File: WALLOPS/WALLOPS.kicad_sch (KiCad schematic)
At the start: 19 parts, among them J1 JST-PH 1x9 Connector - WALLOP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, Q1 AO3401A, U1 VL53L8CX 0 (Zwicky), U2 VL58L8CX 1 (Aristotle), U3 VL53L8CX 3 (Copernicus), U4 VL53L8CX 2 (Brahe), U5 6DOF IMU (Sisko), U6 5V to 3.3V Converter

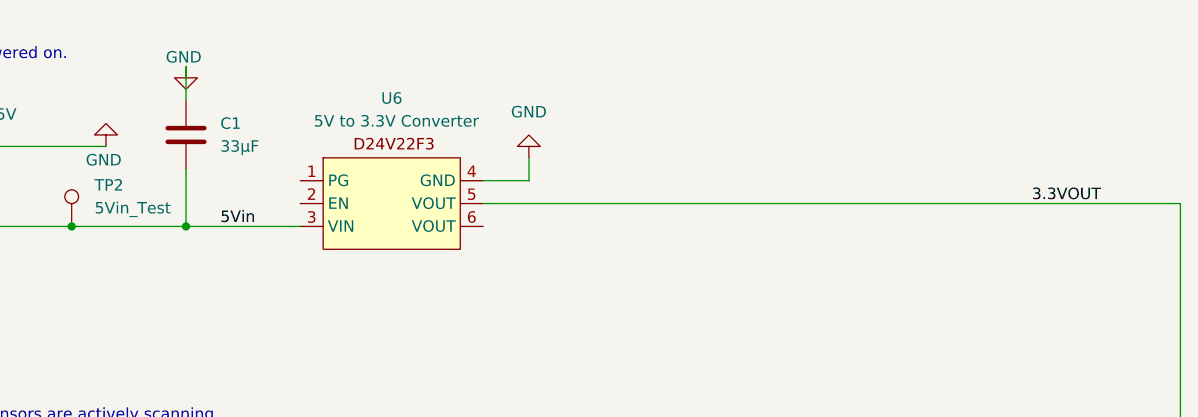
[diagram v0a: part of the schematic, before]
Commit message: Updated capacitors to filter noise and added magnetometer
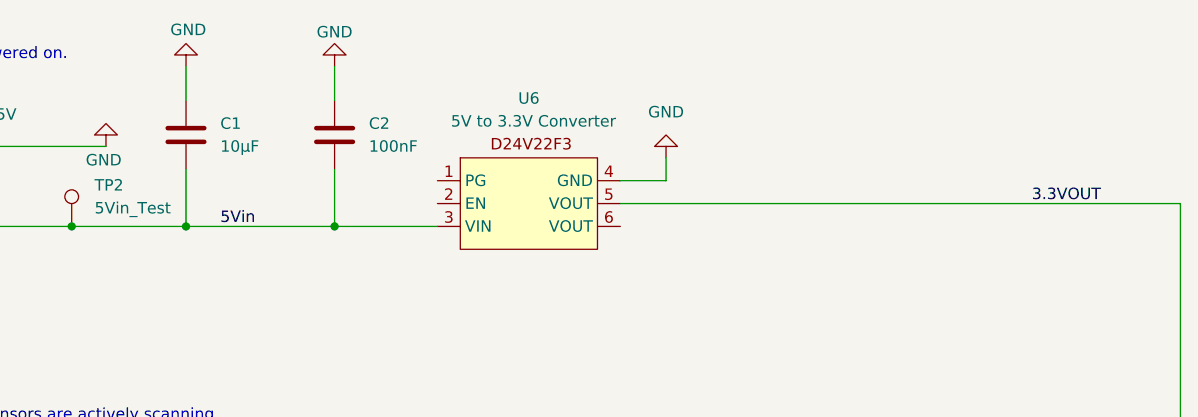
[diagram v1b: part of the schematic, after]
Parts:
- added C2: 100nF, symbol Device:C
- C1: value 33µF -> 10µF
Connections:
- net 5Vin: now also C2.2
- net GND: now also C2.1
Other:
- moved on the sheet: U6
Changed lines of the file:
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@@
 	)
 	(junction
+		(at 153.67 43.18)
+		(diameter 0)
+		(color 0 0 0 0)
+	)
+	(junction
 		(at 90.17 81.28)
 		(diameter 0)
@@
 	(wire
 		(pts
-			(xy 170.18 40.64) (xy 247.65 40.64)
+			(xy 185.42 40.64) (xy 247.65 40.64)
 		)
 		(stroke
@@
 	(wire
 		(pts
+			(xy 153.67 43.18) (xy 165.1 43.18)
+		)
+		(stroke
+			(width 0)
+			(type default)
+		)
+	)
+	(wire
+		(pts
 			(xy 82.55 81.28) (xy 90.17 81.28)
 		)
@@
 	(wire
 		(pts
-			(xy 175.26 35.56) (xy 175.26 38.1)
+			(xy 190.5 35.56) (xy 190.5 38.1)
 		)
 		(stroke
@@
 	(wire
 		(pts
+			(xy 153.67 36.83) (xy 153.67 43.18)
+		)
+		(stroke
+			(width 0)
+			(type default)
+		)
+	)
+	(wire
+		(pts
 			(xy 113.03 100.33) (xy 113.03 101.6)
 		)
@@
 	(wire
 		(pts
+			(xy 153.67 25.4) (xy 153.67 29.21)
+		)
+		(stroke
+			(width 0)
+			(type default)
+		)
+	)
+	(wire
+		(pts
 			(xy 26.67 63.5) (xy 33.02 63.5)
 		)
@@
 	(wire
 		(pts
-			(xy 170.18 38.1) (xy 175.26 38.1)
+			(xy 185.42 38.1) (xy 190.5 38.1)
 		)
 		(stroke
@@
 	(wire
 		(pts
-			(xy 137.16 43.18) (xy 149.86 43.18)
+			(xy 137.16 43.18) (xy 153.67 43.18)
 		)
 		(stroke
@@
 	)
 	(symbol
+		(lib_id "power:GND")
+		(at 153.67 25.4 180)
+		(unit 1)
+		(exclude_from_sim no)
+		(in_bom yes)
+		(on_board yes)
+		(dnp no)
+		(property "Reference" "#PWR03"
+			(at 153.67 19.05 0)
+			(effects
+				(font
+					(size 1.27 1.27)
+				)
+				(hide yes)
+			)
+		)
+		(property "Value" "GND"
+			(at 153.67 21.59 0)
+			(effects
+				(font
+					(size 1.27 1.27)
+				)
+			)
+		)
+		(property "Footprint" ""
+			(at 153.67 25.4 0)
+			(effects
+				(font
+					(size 1.27 1.27)
+				)
+				(hide yes)
+			)
+		)
+		(property "Datasheet" ""
+			(at 153.67 25.4 0)
+			(effects
+				(font
+					(size 1.27 1.27)
+				)
+				(hide yes)
+			)
+		)
+		(property "Description" "Power symbol creates a global label with name \"GND\" , ground"
+			(at 153.67 25.4 0)
+			(effects
+				(font
+					(size 1.27 1.27)
+				)
+				(hide yes)
+			)
+		)
+		(pin "1"
+		)
+		(instances
+			(project ""
+				(path "/a71b320d-cbec-40c8-adfb-8ac61cfef5bf"
+					(reference "#PWR03")
+					(unit 1)
+				)
+			)
+		)
+	)
+	(symbol
 		(lib_id "Device:C")
 		(at 137.16 33.02 0)
@@
 			)
 		)
-		(property "Value" "33µF"
+		(property "Value" "10µF"
 			(at 140.97 34.2899 0)
 			(effects
@@
 	(symbol
 		(lib_id "power:GND")
-		(at 137.16 25.4 0)
+		(at 137.16 25.4 180)
 		(unit 1)
 		(exclude_from_sim no)
@@
 		(dnp no)
 		(property "Reference" "#PWR04"
-			(at 137.16 31.75 0)
+			(at 137.16 19.05 0)
 			(effects
 				(font
@@
 		)
 		(property "Value" "GND"
-			(at 136.906 24.384 0)
+			(at 137.414 21.336 0)
 			(effects
 				(font
@@
 	)
 	(symbol
+		(lib_id "Device:C")
+		(at 153.67 33.02 0)
+		(unit 1)
+		(exclude_from_sim no)
+		(in_bom yes)
+		(on_board yes)
+		(dnp no)
+		(fields_autoplaced yes)
+		(property "Reference" "C2"
+			(at 157.48 31.7499 0)
+			(effects
+				(font
+					(size 1.27 1.27)
+				)
+				(justify left)
+			)
+		)
+		(property "Value" "100nF"
+			(at 157.48 34.2899 0)
+			(effects
+				(font
+					(size 1.27 1.27)
+				)
+				(justify left)
+			)
+		)
+		(property "Footprint" ""
+			(at 154.6352 36.83 0)
+			(effects
+				(font
+					(size 1.27 1.27)
+				)
+				(hide yes)
+			)
+		)
+		(property "Datasheet" "~"
+			(at 153.67 33.02 0)
+			(effects
+				(font
+					(size 1.27 1.27)
+				)
+				(hide yes)
+			)
+		)
+		(property "Description" "Unpolarized capacitor"
+			(at 153.67 33.02 0)
+			(effects
+				(font
+					(size 1.27 1.27)
+				)
+				(hide yes)
+			)
+		)
+		(pin "2"
+		)
+		(pin "1"
+		)
+		(instances
+			(project ""
+				(path "/a71b320d-cbec-40c8-adfb-8ac61cfef5bf"
+					(reference "C2")
+					(unit 1)
+				)
+			)
+		)
+	)
+	(symbol
 		(lib_id "Device:LED")
 		(at 110.49 73.66 180)
@@
 	(symbol
 		(lib_id "RockSat_Sym:Pololu_D24V22F3")
-		(at 160.02 40.64 0)
+		(at 175.26 40.64 0)
 		(unit 1)
 		(exclude_from_sim no)
@@
 		(dnp no)
 		(property "Reference" "U6"
-			(at 160.02 28.956 0)
+			(at 175.26 28.956 0)
 			(effects
 				(font
@@
 		)
 		(property "Value" "5V to 3.3V Converter"
-			(at 160.528 31.496 0)
+			(at 175.768 31.496 0)
 			(effects
 				(font
@@
 		)
 		(property "Footprint" "RockSat:D24V22F3"
-			(at 160.02 40.64 0)
+			(at 175.26 40.64 0)
 			(effects
 				(font
@@
 		)
 		(property "Datasheet" ""
-			(at 160.02 40.64 0)
+			(at 175.26 40.64 0)
 			(effects
 				(font
@@
 		)
 		(property "Description" ""
-			(at 160.02 40.64 0)
+			(at 175.26 40.64 0)
 			(effects
 				(font
@@
 	(symbol
 		(lib_id "power:GND")
-		(at 175.26 35.56 180)
+		(at 190.5 35.56 180)
 		(unit 1)
 		(exclude_from_sim no)
@@
 		(fields_autoplaced yes)
 		(property "Reference" "#PWR02"
-			(at 175.26 29.21 0)
+			(at 190.5 29.21 0)
 			(effects
 				(font
@@
 		)
 		(property "Value" "GND"
-			(at 175.26 30.48 0)
+			(at 190.5 30.48 0)
 			(effects
 				(font
@@
 		)
 		(property "Footprint" ""
-			(at 175.26 35.56 0)
+			(at 190.5 35.56 0)
 			(effects
 				(font
@@
 		)
 		(property "Datasheet" ""
-			(at 175.26 35.56 0)
+			(at 190.5 35.56 0)
 			(effects
 				(font
@@
 		)
 		(property "Description" "Power symbol creates a global label with name \"GND\" , ground"
-			(at 175.26 35.56 0)
+			(at 190.5 35.56 0)
 			(effects
 				(font

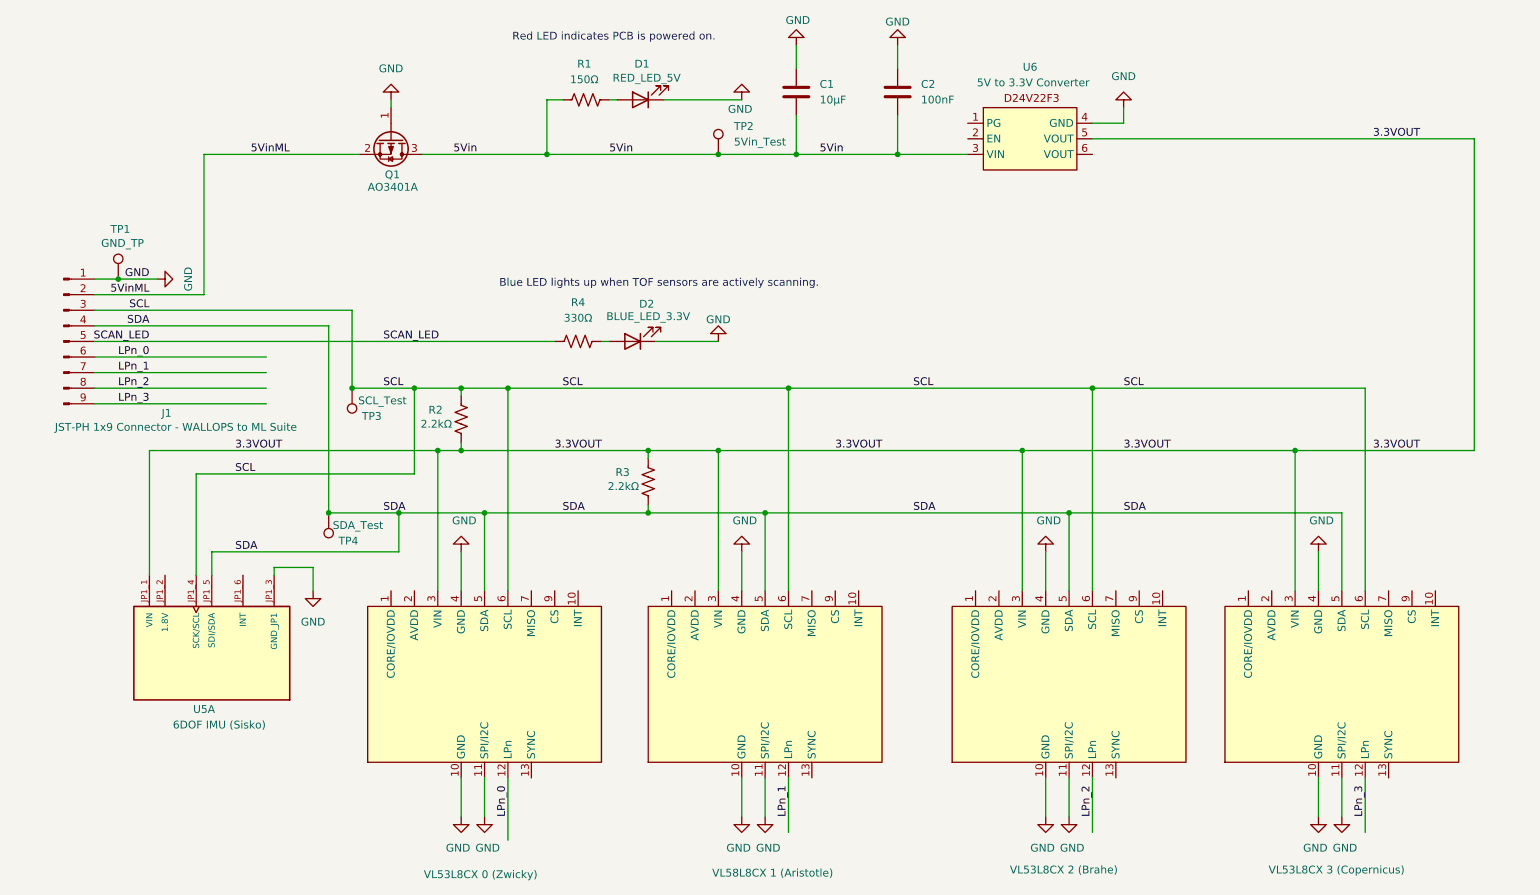
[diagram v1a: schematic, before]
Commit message: Added Magnetometer to schematic
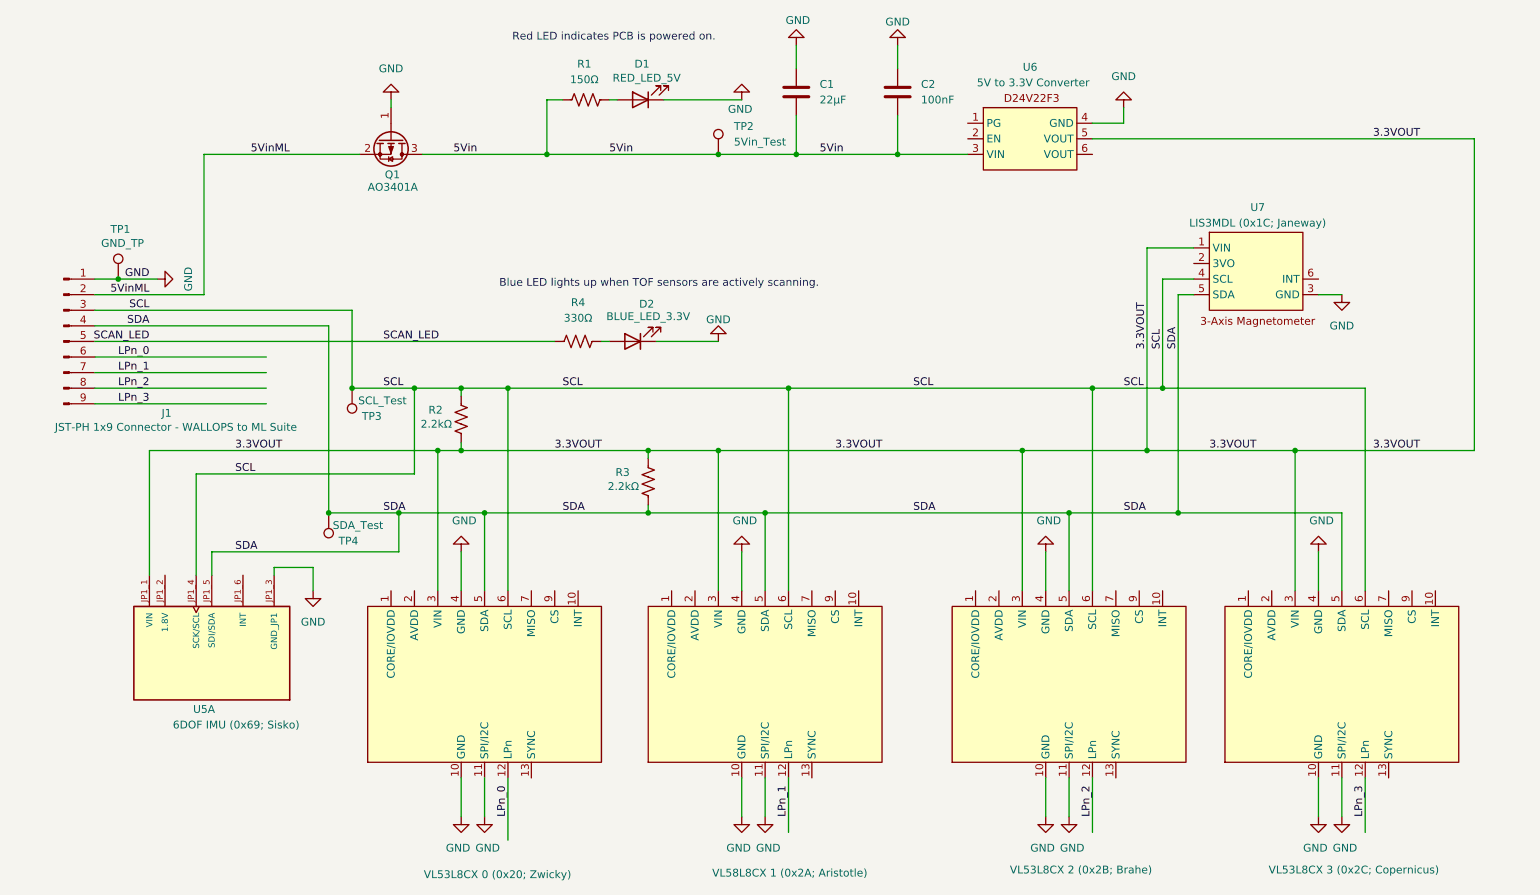
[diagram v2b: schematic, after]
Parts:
- added U7: LIS3MDL (0x1C; Janeway), symbol RockSat_Sym:LIS3MDL_Magnetometer
- C1: value 10µF -> 22µF
- U1: value VL53L8CX 0 (Zwicky) -> VL53L8CX 0 (0x20; Zwicky)
- U2: value VL58L8CX 1 (Aristotle) -> VL58L8CX 1 (0x2A; Aristotle)
- U3: value VL53L8CX 3 (Copernicus) -> VL53L8CX 3 (0x2C; Copernicus)
- U4: value VL53L8CX 2 (Brahe) -> VL53L8CX 2 (0x2B; Brahe)
- U5: value 6DOF IMU (Sisko) -> 6DOF IMU (0x69; Sisko)
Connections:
- net 3.3VOUT: now also U7.1 (VIN)
- net GND: now also U7.3 (GND)
- net SCL: now also U7.4 (SCL)
- net SDA: now also U7.5 (SDA)

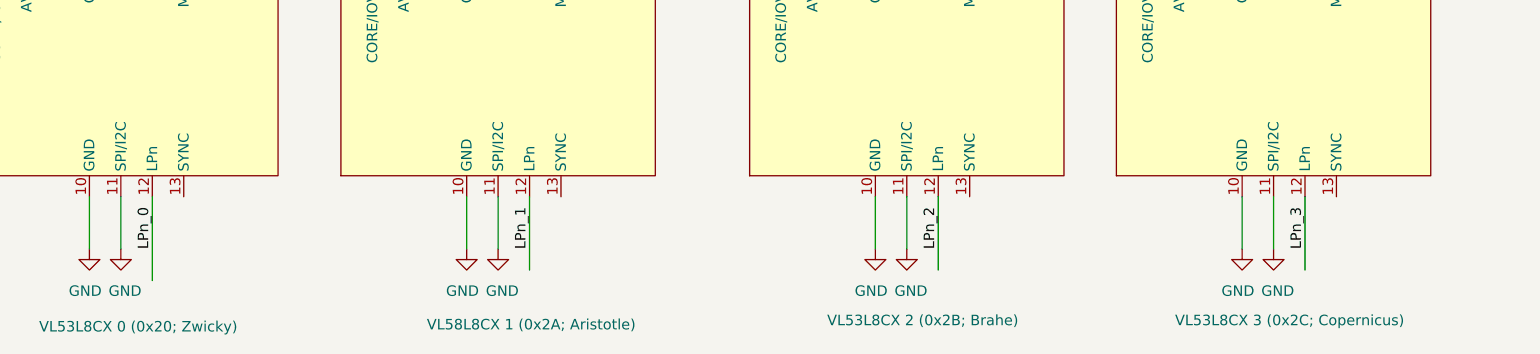
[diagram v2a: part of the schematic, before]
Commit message: Added individual TOF LPn pins to WALLOPS PCB
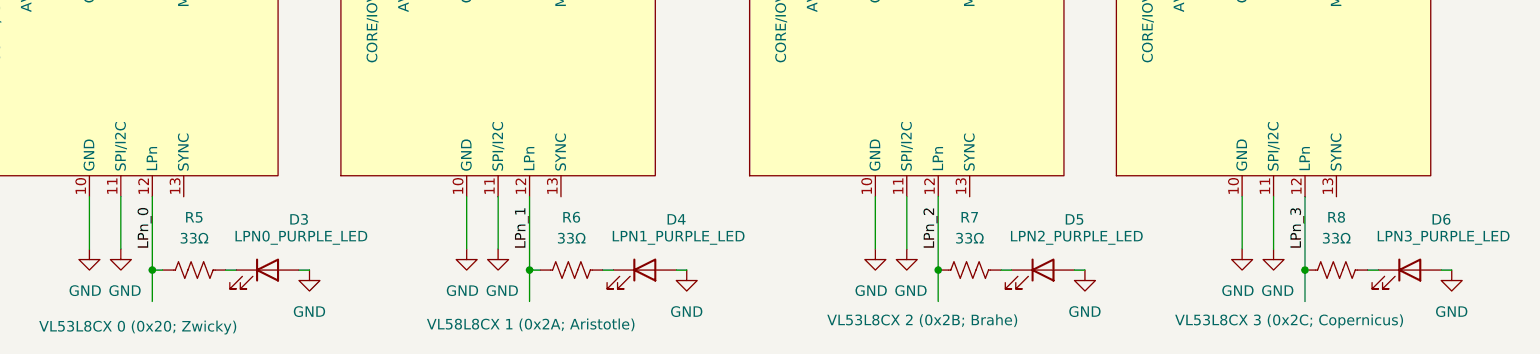
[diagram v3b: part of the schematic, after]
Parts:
- added D3: LPN0_PURPLE_LED, LED_SMD:LED_0201_0603Metric_Pad0.64x0.40mm_HandSolder, symbol Device:LED
- added D4: LPN1_PURPLE_LED, LED_SMD:LED_0201_0603Metric_Pad0.64x0.40mm_HandSolder, symbol Device:LED
- added D5: LPN2_PURPLE_LED, LED_SMD:LED_0201_0603Metric_Pad0.64x0.40mm_HandSolder, symbol Device:LED
- added D6: LPN3_PURPLE_LED, LED_SMD:LED_0201_0603Metric_Pad0.64x0.40mm_HandSolder, symbol Device:LED
- added R5, R6, R7, R8: 33Ω, Resistor_SMD:R_0805_2012Metric_Pad1.20x1.40mm_HandSolder, symbol Device:R_US
- C1: footprint Capacitor_SMD:C_0805_2012Metric -> Capacitor_SMD:C_0805_2012Metric_Pad1.18x1.45mm_HandSolder
- C2: footprint (none) -> Capacitor_SMD:C_0805_2012Metric_Pad1.18x1.45mm_HandSolder
- D1, D2: footprint LED_SMD:LED_0805_2012Metric -> LED_SMD:LED_0805_2012Metric_Pad1.15x1.40mm_HandSolder
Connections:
- net GND: now also D3.2 (A), D4.2 (A), D5.2 (A), D6.2 (A)
- net LPn_0: now also R5.1
- net LPn_1: now also R6.1
- net LPn_2: now also R7.1
- net LPn_3: now also R8.1
- new net: D3.1 (K), R5.2
- new net: D6.1 (K), R8.2
- new net: D4.1 (K), R6.2
- new net: D5.1 (K), R7.2
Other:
- title: WALLOPS 4x(8x8) Channel LiDAR Scan -> WALLOPS 256 Channel LiDAR Scan

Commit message: Fixed WALLOPS JST-PH footprint; switched 0603 LEDs back to 0805
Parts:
- D3, D4, D5, D6: footprint LED_SMD:LED_0201_0603Metric_Pad0.64x0.40mm_HandSolder -> LED_SMD:LED_0805_2012Metric_Pad1.15x1.40mm_HandSolder
- J1: footprint Connector_JST:JST_PH_S9B-PH-K_1x09_P2.00mm_Horizontal -> Connector_JST:JST_PH_S9B-PH-SM4-TB_1x09-1MP_P2.00mm_Horizontal
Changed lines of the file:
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@@
 			)
 		)
-		(property "Footprint" "Connector_JST:JST_PH_S9B-PH-K_1x09_P2.00mm_Horizontal"
+		(property "Footprint" "Connector_JST:JST_PH_S9B-PH-SM4-TB_1x09-1MP_P2.00mm_Horizontal"
 			(at 17.78 73.66 0)
 			(effects
@@
 			)
 		)
-		(property "Footprint" "LED_SMD:LED_0201_0603Metric_Pad0.64x0.40mm_HandSolder"
+		(property "Footprint" "LED_SMD:LED_0805_2012Metric_Pad1.15x1.40mm_HandSolder"
 			(at 104.14 153.67 0)
 			(effects
@@
 			)
 		)
-		(property "Footprint" "LED_SMD:LED_0201_0603Metric_Pad0.64x0.40mm_HandSolder"
+		(property "Footprint" "LED_SMD:LED_0805_2012Metric_Pad1.15x1.40mm_HandSolder"
 			(at 242.57 153.67 0)
 			(effects
@@
 			)
 		)
-		(property "Footprint" "LED_SMD:LED_0201_0603Metric_Pad0.64x0.40mm_HandSolder"
+		(property "Footprint" "LED_SMD:LED_0805_2012Metric_Pad1.15x1.40mm_HandSolder"
 			(at 149.86 153.67 0)
 			(effects
@@
 			)
 		)
-		(property "Footprint" "LED_SMD:LED_0201_0603Metric_Pad0.64x0.40mm_HandSolder"
+		(property "Footprint" "LED_SMD:LED_0805_2012Metric_Pad1.15x1.40mm_HandSolder"
 			(at 198.12 153.67 0)
 			(effects
